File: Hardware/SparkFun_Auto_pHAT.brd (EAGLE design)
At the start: 65.1 x 57 mm, 233 parts, among them J11 EXT MTR PWR, J18 ISP, J2 RASPBERRYPI-40-PIN-GPIO_SMD_S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, J20 USB C, J23 CORTEX_JTAG_DEBUG_PTH, J7 EXT SERVO PWR, J8 EXT 5V PWR, Q1 310mA/60V/1.6Ω, Q23 20V/0.2A/8MHz/1.2Ω/1Vth, Q24 20V/0.2A/8MHz/1.2Ω/1Vth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

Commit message: TP19 (3.3V) moved to bottom, to expose bStop
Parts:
- flipped TP19 to the top
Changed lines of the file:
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@@
 <layer number="18" name="Vias" color="2" fill="1" visible="yes" active="yes"/>
 <layer number="19" name="Unrouted" color="6" fill="1" visible="yes" active="yes"/>
-<layer number="20" name="Dimension" color="24" fill="1" visible="yes" active="yes"/>
-<layer number="21" name="tPlace" color="16" fill="1" visible="yes" active="yes"/>
-<layer number="22" name="bPlace" color="14" fill="1" visible="yes" active="yes"/>
+<layer number="20" name="Dimension" color="24" fill="1" visible="no" active="yes"/>
+<layer number="21" name="tPlace" color="16" fill="1" visible="no" active="yes"/>
+<layer number="22" name="bPlace" color="14" fill="1" visible="no" active="yes"/>
 <layer number="23" name="tOrigins" color="15" fill="1" visible="yes" active="yes"/>
 <layer number="24" name="bOrigins" color="15" fill="1" visible="yes" active="yes"/>
@@
 <layer number="28" name="bValues" color="7" fill="1" visible="no" active="yes"/>
 <layer number="29" name="tStop" color="7" fill="3" visible="no" active="yes"/>
-<layer number="30" name="bStop" color="7" fill="6" visible="no" active="yes"/>
+<layer number="30" name="bStop" color="7" fill="6" visible="yes" active="yes"/>
 <layer number="31" name="tCream" color="7" fill="4" visible="no" active="yes"/>
 <layer number="32" name="bCream" color="7" fill="5" visible="no" active="yes"/>
@@
 <layer number="43" name="vRestrict" color="2" fill="10" visible="no" active="yes"/>
 <layer number="44" name="Drills" color="7" fill="1" visible="no" active="yes"/>
-<layer number="45" name="Holes" color="7" fill="1" visible="yes" active="yes"/>
+<layer number="45" name="Holes" color="7" fill="1" visible="no" active="yes"/>
 <layer number="46" name="Milling" color="3" fill="1" visible="no" active="yes"/>
 <layer number="47" name="Measures" color="7" fill="1" visible="no" active="yes"/>
 <layer number="48" name="Document" color="13" fill="7" visible="no" active="yes"/>
-<layer number="49" name="Reference" color="13" fill="1" visible="yes" active="yes"/>
+<layer number="49" name="Reference" color="13" fill="1" visible="no" active="yes"/>
 <layer number="50" name="dxf" color="7" fill="1" visible="no" active="yes"/>
-<layer number="51" name="tDocu" color="6" fill="1" visible="yes" active="yes"/>
+<layer number="51" name="tDocu" color="6" fill="1" visible="no" active="yes"/>
 <layer number="52" name="bDocu" color="7" fill="1" visible="no" active="yes"/>
 <layer number="91" name="Nets" color="2" fill="1" visible="no" active="no"/>
@@
 <element name="TP17" library="SparkFun-Connectors" package="PAD.03X.04" value="" x="15.24" y="6.35" smashed="yes" rot="MR0"/>
 <element name="TP18" library="SparkFun-Connectors" package="PAD.03X.04" value="" x="12.7" y="6.35" smashed="yes" rot="MR0"/>
-<element name="TP19" library="SparkFun-Connectors" package="TP_15TH" value="" x="22.86" y="39.37" smashed="yes" rot="MR0"/>
+<element name="TP19" library="SparkFun-Connectors" package="TP_15TH" value="" x="22.86" y="39.37" smashed="yes"/>
 </elements>
 <signals>
@@
 <wire x1="22.86" y1="45.72" x2="20.92198125" y2="47.65801875" width="0.508" layer="16"/>
 <wire x1="22.86" y1="45.72" x2="22.86" y2="42.4332375" width="0.508" layer="16"/>
-<wire x1="22.86" y1="42.4332375" x2="22.86" y2="39.37" width="0.508" layer="16"/>
-<wire x1="22.86" y1="39.37" x2="22.86" y2="35.56" width="0.508" layer="16"/>
 <wire x1="22.86" y1="35.56" x2="22.86" y2="31.168340625" width="0.508" layer="16"/>
 <wire x1="22.86" y1="31.168340625" x2="22.86" y2="26.67" width="0.508" layer="16"/>
@@
 <wire x1="39.4614375" y1="37.9196625" x2="34.9148375" y2="42.4662625" width="0.508" layer="16"/>
 <wire x1="11.85" y1="34.29" x2="11.85" y2="35.98" width="0.508" layer="1"/>
-<wire x1="15.24" y1="39.37" x2="22.86" y2="39.37" width="0.508" layer="1"/>
 <wire x1="11.85" y1="35.98" x2="15.24" y2="39.37" width="0.508" layer="1"/>
 <wire x1="9.9" y1="32.385" x2="11.2293375" y2="32.385" width="0.508" layer="1"/>
@@
 <wire x1="29.0195" y1="33.566478125" x2="28.463240625" y2="33.566478125" width="0.254" layer="1"/>
 <wire x1="28.463240625" y1="33.566478125" x2="27.853640625" y2="33.566478125" width="0.254" layer="1"/>
-<wire x1="22.86" y1="35.56" x2="28.44038125" y2="35.56" width="0.2032" layer="16"/>
+<wire x1="28.44038125" y1="35.56" x2="22.86" y2="35.56" width="0.2032" layer="16"/>
 <wire x1="28.44038125" y1="35.56" x2="28.4607" y2="35.53968125" width="0.2032" layer="16"/>
 <via x="28.4607" y="35.53968125" extent="1-16" drill="0.381"/>
@@
 <wire x1="17.526" y1="3.175" x2="17.526" y2="7.426959375" width="0.254" layer="16"/>
 <contactref element="TP19" pad="P$1"/>
+<wire x1="22.86" y1="42.4332375" x2="22.86" y2="39.37" width="0.508" layer="16"/>
+<wire x1="22.86" y1="35.56" x2="22.86" y2="39.37" width="0.508" layer="16"/>
+<wire x1="15.24" y1="39.37" x2="22.86" y2="39.37" width="0.508" layer="1"/>
 </signal>
 <signal name="5V">

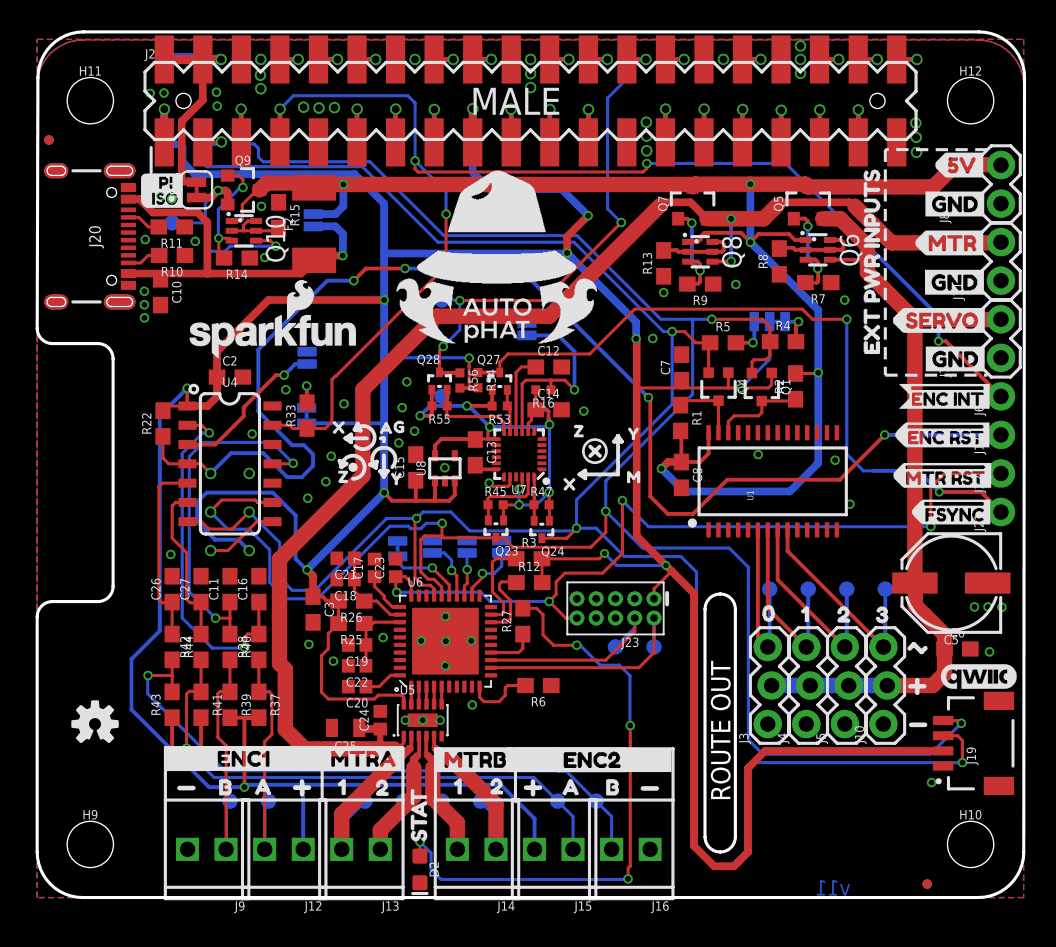
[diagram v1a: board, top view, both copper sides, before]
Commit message: v12
-moved stat LED to side for easier rework and better visibility
-added holes to let air through to SHIM Fan (when it sits flush up to the PCB, there is no room for airflow)
-bumped version to v12 in copper and all 3 sheets in sch
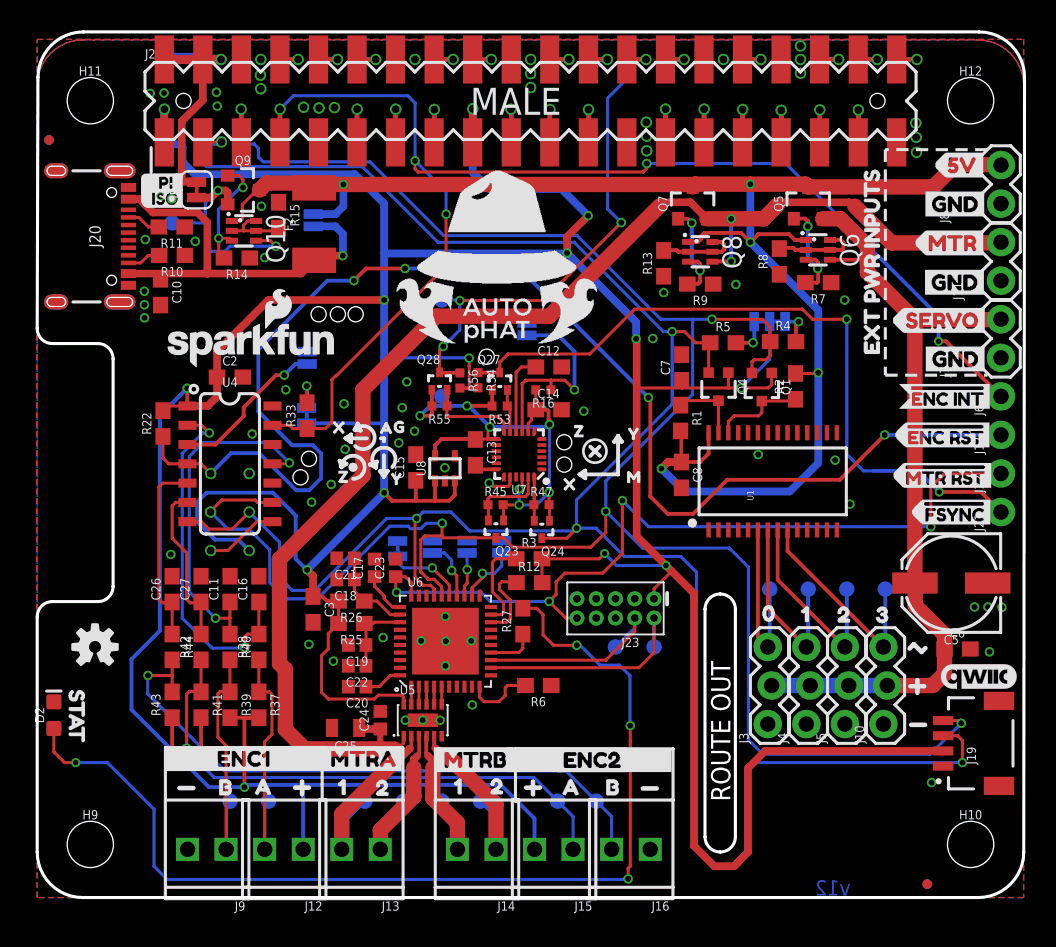
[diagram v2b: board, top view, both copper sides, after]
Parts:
- added U$18, U$19: (no value), autophat:1X06_2.54_SCREWTERM_PIN_REF
- moved D2 26.2 mm to (1.10, 12.0), turned to 90 degrees
- moved U$29 25.5 mm to (2.61, 14.6), turned to 270 degrees
- moved LOGO2 5.08 mm to (3.81, 16.5)
- moved LOGO4 1.56 mm to (14.2, 36.4)
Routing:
- net N$27: track 39.4 -> 68.2 mm
- net !ENC_RST: track 86.6 -> 88.9 mm
- net ENC1B_FILTERED: track 23.6 -> 23.1 mm
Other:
- board text added: "v12"
- board text removed: "v11"

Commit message: Adjusted screwpin terminal fp and locations to work with 1x2s and 1x6s
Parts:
- J13, J14, J16, J9: device SparkFun-Connectors:1X02_2.54_SCREWTERM -> autophat:1X02_2.54_SCREWTERM_LG_DRILL
- moved J9 0.10 mm to (12.3, 3.17)
- moved J13 0.10 mm to (22.7, 3.17)
- moved J14 0.10 mm to (30.1, 3.17)
- moved J16 0.10 mm to (40.5, 3.17)

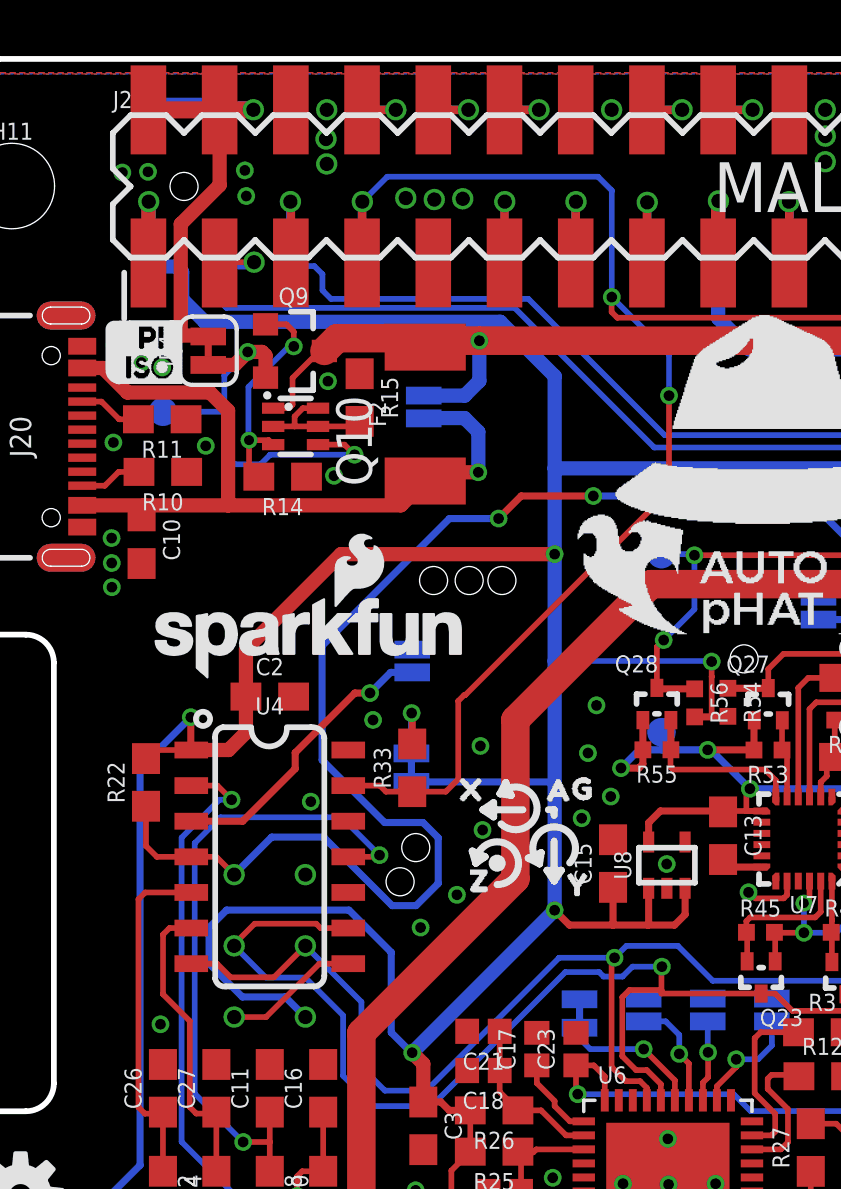
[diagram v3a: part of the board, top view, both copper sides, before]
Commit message: Design Review changes
-Decreased 5V trace by Pi 40pin 5V header pad, to avoid tStop overlap.
-Decreased SDA and SCL trace width to 0.007 inch near pi header (in the uppder left of board) to avoid bStop overlap on those traces.
-Added Voltage ranges to pin labels on EXT power inputs (bottom silk labels only)
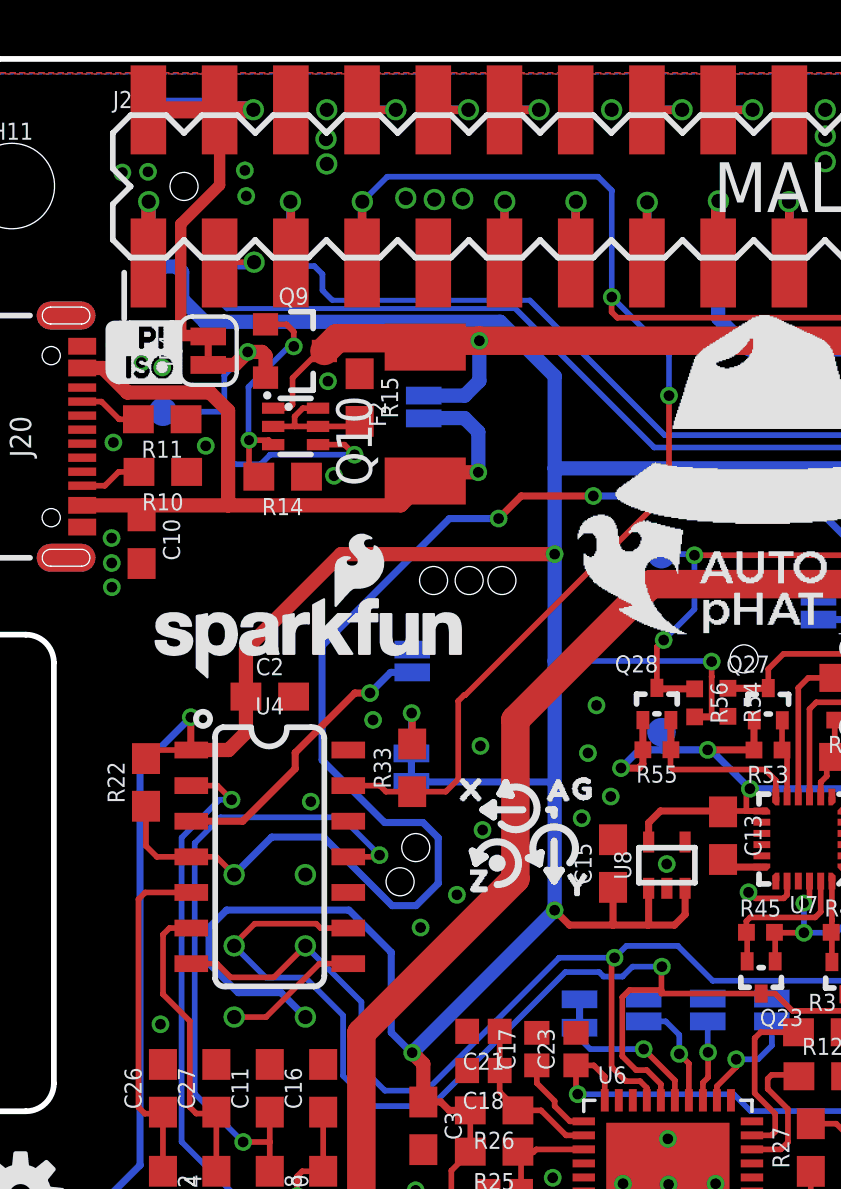
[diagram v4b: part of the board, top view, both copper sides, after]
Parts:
- removed U$54: (no value), buzzard_labels (6):MTR4
- removed U$55: (no value), buzzard_labels (6):SERVO5
- added U$30: (no value), buzzard_labels:SRV_5#6V1
- added U$38: (no value), buzzard_labels (1):MTR_5#9V0
- moved U$52 1.91 mm to (53.1, 48.8)
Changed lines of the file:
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@@
 <rectangle x1="30.99308125" y1="8.265159375" x2="34.4551" y2="9.903459375" layer="21"/>
 <rectangle x1="26.14168125" y1="8.2677" x2="26.5938" y2="9.903459375" layer="21"/>
-<wire x1="62.6237" y1="49.278540625" x2="55.8927" y2="49.278540625" width="0.2032" layer="22" style="shortdash"/>
-<wire x1="55.87491875" y1="49.273459375" x2="55.87491875" y2="34.414459375" width="0.2032" layer="22" style="shortdash"/>
-<wire x1="62.61608125" y1="34.417" x2="55.88508125" y2="34.417" width="0.2032" layer="22" style="shortdash"/>
+<wire x1="62.6237" y1="49.278540625" x2="53.9877" y2="49.278540625" width="0.2032" layer="22" style="shortdash"/>
+<wire x1="53.96991875" y1="49.273459375" x2="53.96991875" y2="34.414459375" width="0.2032" layer="22" style="shortdash"/>
+<wire x1="62.61608125" y1="34.417" x2="53.98008125" y2="34.417" width="0.2032" layer="22" style="shortdash"/>
 <wire x1="23.9268" y1="0.04571875" x2="23.9268" y2="5.694678125" width="0.2032" layer="22"/>
 <wire x1="23.9268" y1="5.694678125" x2="8.671559375" y2="5.712459375" width="0.2032" layer="22"/>
@@
 <element name="U$39" library="buzzard_labels (6)" package="IMU_ADR9" value="" x="31.75761875" y="37.4396" smashed="yes" rot="MR0"/>
 <element name="U$51" library="buzzard_labels (7)" package="MTR_ADR0" value="" x="31.42488125" y="26.5684" smashed="yes" rot="MR0"/>
-<element name="U$52" library="buzzard_labels (1)" package="EXT_PWR_INPUTS3" value="" x="55.01131875" y="48.8442" smashed="yes" rot="MR270"/>
+<element name="U$52" library="buzzard_labels (1)" package="EXT_PWR_INPUTS3" value="" x="53.10631875" y="48.8442" smashed="yes" rot="MR270"/>
 <element name="U$53" library="buzzard_labels (6)" package="5V3" value="" x="63.21298125" y="48.247296875" smashed="yes" rot="MR0"/>
-<element name="U$54" library="buzzard_labels (6)" package="MTR4" value="" x="63.2587" y="43.113959375" smashed="yes" rot="MR0"/>
-<element name="U$55" library="buzzard_labels (6)" package="SERVO5" value="" x="63.162178125" y="38.003478125" smashed="yes" rot="MR0"/>
 <element name="U$56" library="buzzard_labels (6)" package="#ENC_RST6" value="" x="63.439040625" y="30.490159375" smashed="yes" rot="MR0"/>
 <element name="U$57" library="buzzard_labels (6)" package="#MTR_RST7" value="" x="63.535559375" y="27.810459375" smashed="yes" rot="MR0"/>
@@
 <element name="U$18" library="autophat" package="1X06_2.54_SCREWTERM_PIN_REF" value="" x="27.686" y="3.175" smashed="yes"/>
 <element name="U$19" library="autophat" package="1X06_2.54_SCREWTERM_PIN_REF" value="" x="9.906" y="3.175" smashed="yes"/>
+<element name="U$30" library="buzzard_labels" package="SRV_5#6V1" value="" x="63.1698" y="37.9984" smashed="yes" rot="MR0"/>
+<element name="U$38" library="buzzard_labels (1)" package="MTR_5#9V0" value="" x="63.2714" y="43.1292" smashed="yes" rot="MR0"/>
 </elements>
 <signals>
@@
 <wire x1="44.45" y1="38.1" x2="47.787559375" y2="38.1" width="0.2032" layer="1"/>
 <wire x1="48.291378125" y1="37.59618125" x2="48.291378125" y2="36.62171875" width="0.2032" layer="1"/>
-<wire x1="21.9227375" y1="48.475903125" x2="14.884396875" y2="48.475903125" width="0.2032" layer="16"/>
-<wire x1="21.9227375" y1="48.475903125" x2="26.7843" y2="43.614340625" width="0.2032" layer="16"/>
+<wire x1="21.9735375" y1="48.425103125" x2="14.935196875" y2="48.425103125" width="0.1778" layer="16"/>
+<wire x1="21.9735375" y1="48.425103125" x2="26.7843" y2="43.614340625" width="0.2032" layer="16"/>
 <wire x1="26.7843" y1="43.614340625" x2="35.5727" y2="43.614340625" width="0.2032" layer="16"/>
 <wire x1="35.5727" y1="43.614340625" x2="41.087040625" y2="38.1" width="0.2032" layer="16"/>
@@
 <wire x1="13.4366" y1="51.943" x2="13.4366" y2="49.6439" width="0.3048" layer="16"/>
 <wire x1="13.4366" y1="49.6439" x2="13.452" y2="49.6285" width="0.3048" layer="16"/>
-<wire x1="14.884396875" y1="48.475903125" x2="14.5796" y2="48.7807" width="0.2032" layer="16"/>
+<wire x1="14.935196875" y1="48.425103125" x2="14.5796" y2="48.7807" width="0.2032" layer="16"/>
 <wire x1="14.2879" y1="49.6439" x2="13.4366" y2="49.6439" width="0.2032" layer="16"/>
 <wire x1="14.5796" y1="48.7807" x2="14.5796" y2="49.3522" width="0.2032" layer="16"/>
@@
 <wire x1="41.8338" y1="37.2872" x2="42.6491375" y2="37.2872" width="0.2032" layer="1"/>
 <wire x1="43.3857375" y1="36.5506" x2="44.3366" y2="36.5506" width="0.2032" layer="1"/>
-<wire x1="26.410921875" y1="43.17491875" x2="21.42998125" y2="48.155859375" width="0.2032" layer="16"/>
+<wire x1="26.410921875" y1="43.17491875" x2="21.45538125" y2="48.130459375" width="0.2032" layer="16"/>
 <wire x1="26.410921875" y1="43.17491875" x2="35.372040625" y2="43.17491875" width="0.2032" layer="16"/>
 <wire x1="44.3366" y1="36.5506" x2="44.236878125" y2="36.450878125" width="0.2032" layer="1"/>
@@
 <wire x1="38.694359375" y1="22.468840625" x2="36.83" y2="24.3332" width="0.2032" layer="16"/>
 <contactref element="J2" pad="3B"/>
-<wire x1="21.42998125" y1="48.155859375" x2="11.153140625" y2="48.155859375" width="0.2032" layer="16"/>
-<wire x1="11.153140625" y1="48.155859375" x2="10.912" y2="48.397" width="0.2032" layer="16"/>
+<wire x1="21.45538125" y1="48.130459375" x2="11.178540625" y2="48.130459375" width="0.1778" layer="16"/>
+<wire x1="11.178540625" y1="48.130459375" x2="10.912" y2="48.397" width="0.2032" layer="16"/>
 <wire x1="10.912" y1="48.397" x2="10.912" y2="49.6285" width="0.2032" layer="16"/>
 <wire x1="12.1412" y1="49.784" x2="11.9857" y2="49.6285" width="0.2032" layer="16"/>
@@
 <wire x1="17.7520625" y1="31.247078125" x2="22.7812625" y2="31.247078125" width="0.254" layer="16"/>
 <wire x1="22.7812625" y1="31.247078125" x2="22.86" y2="31.168340625" width="0.254" layer="16"/>
-<wire x1="13.97" y1="22.86" x2="13.25118125" y2="23.57881875" width="0.254" layer="16"/>
-<wire x1="13.25118125" y1="23.57881875" x2="11.7221" y2="23.57881875" width="0.254" layer="16"/>
-<wire x1="11.7221" y1="23.57881875" x2="10.53591875" y2="24.765" width="0.254" layer="16"/>
+<wire x1="13.97" y1="22.86" x2="13.09878125" y2="23.73121875" width="0.254" layer="16"/>
+<wire x1="13.09878125" y1="23.73121875" x2="11.5697" y2="23.73121875" width="0.254" layer="16"/>
+<wire x1="11.5697" y1="23.73121875" x2="10.53591875" y2="24.765" width="0.254" layer="16"/>
 <wire x1="10.53591875" y1="24.765" x2="10.53591875" y2="26.052778125" width="0.254" layer="16"/>
 <wire x1="17.033240625" y1="25.16631875" x2="17.033240625" y2="22.311359375" width="0.254" layer="16"/>
@@
 <wire x1="8.372" y1="55.3435" x2="10.912" y2="55.3435" width="0.6096" layer="16"/>
 <wire x1="10.912" y1="55.3435" x2="11.0359" y2="55.2196" width="0.6096" layer="16"/>
-<wire x1="9.525" y1="47.1678" x2="9.525" y2="51.14469375" width="0.508" layer="1"/>
-<wire x1="10.912" y1="55.2165" x2="10.912" y2="52.53169375" width="0.508" layer="1"/>
-<wire x1="10.912" y1="52.53169375" x2="9.525" y2="51.14469375" width="0.508" layer="1"/>
+<wire x1="9.525" y1="47.1678" x2="9.525" y2="51.14469375" width="0.4064" layer="1"/>
+<wire x1="10.912" y1="55.2165" x2="10.912" y2="52.53169375" width="0.4064" layer="1"/>
+<wire x1="10.912" y1="52.53169375" x2="9.525" y2="51.14469375" width="0.4064" layer="1"/>
 <wire x1="10.505440625" y1="47.134778125" x2="10.47241875" y2="47.1678" width="0.508" layer="1"/>
-<wire x1="10.47241875" y1="47.1678" x2="9.525" y2="47.1678" width="0.508" layer="1"/>
+<wire x1="10.47241875" y1="47.1678" x2="9.525" y2="47.1678" width="0.4064" layer="1"/>
 </signal>
 <signal name="N$24">
